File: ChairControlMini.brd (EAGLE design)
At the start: 150 x 84 mm, 36 parts, among them J1 Digital_0_7, J2 Analog, J3 Digital_8_13, J4 Analog, J5 Digital_0_7, SW1 SWITCH-DPDT3, X1 INPUT, X2 OUTPUT, X4 INPUT

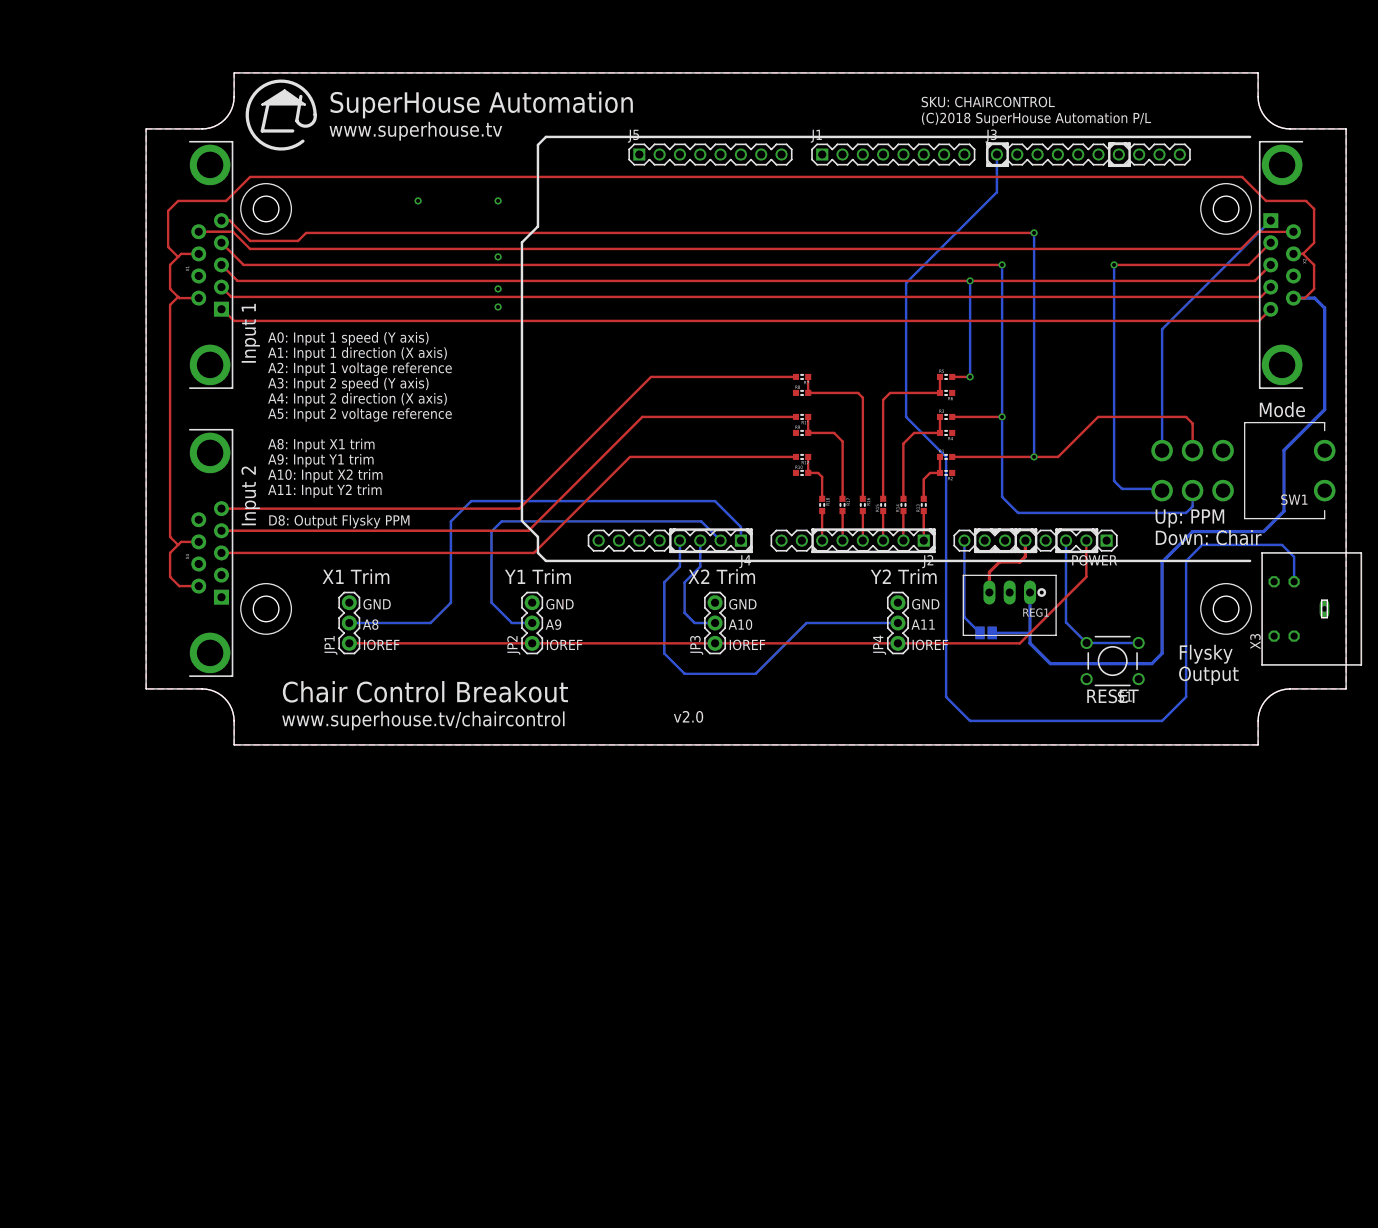
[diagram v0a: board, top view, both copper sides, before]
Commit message: Added CAN interface and removed second joystick input
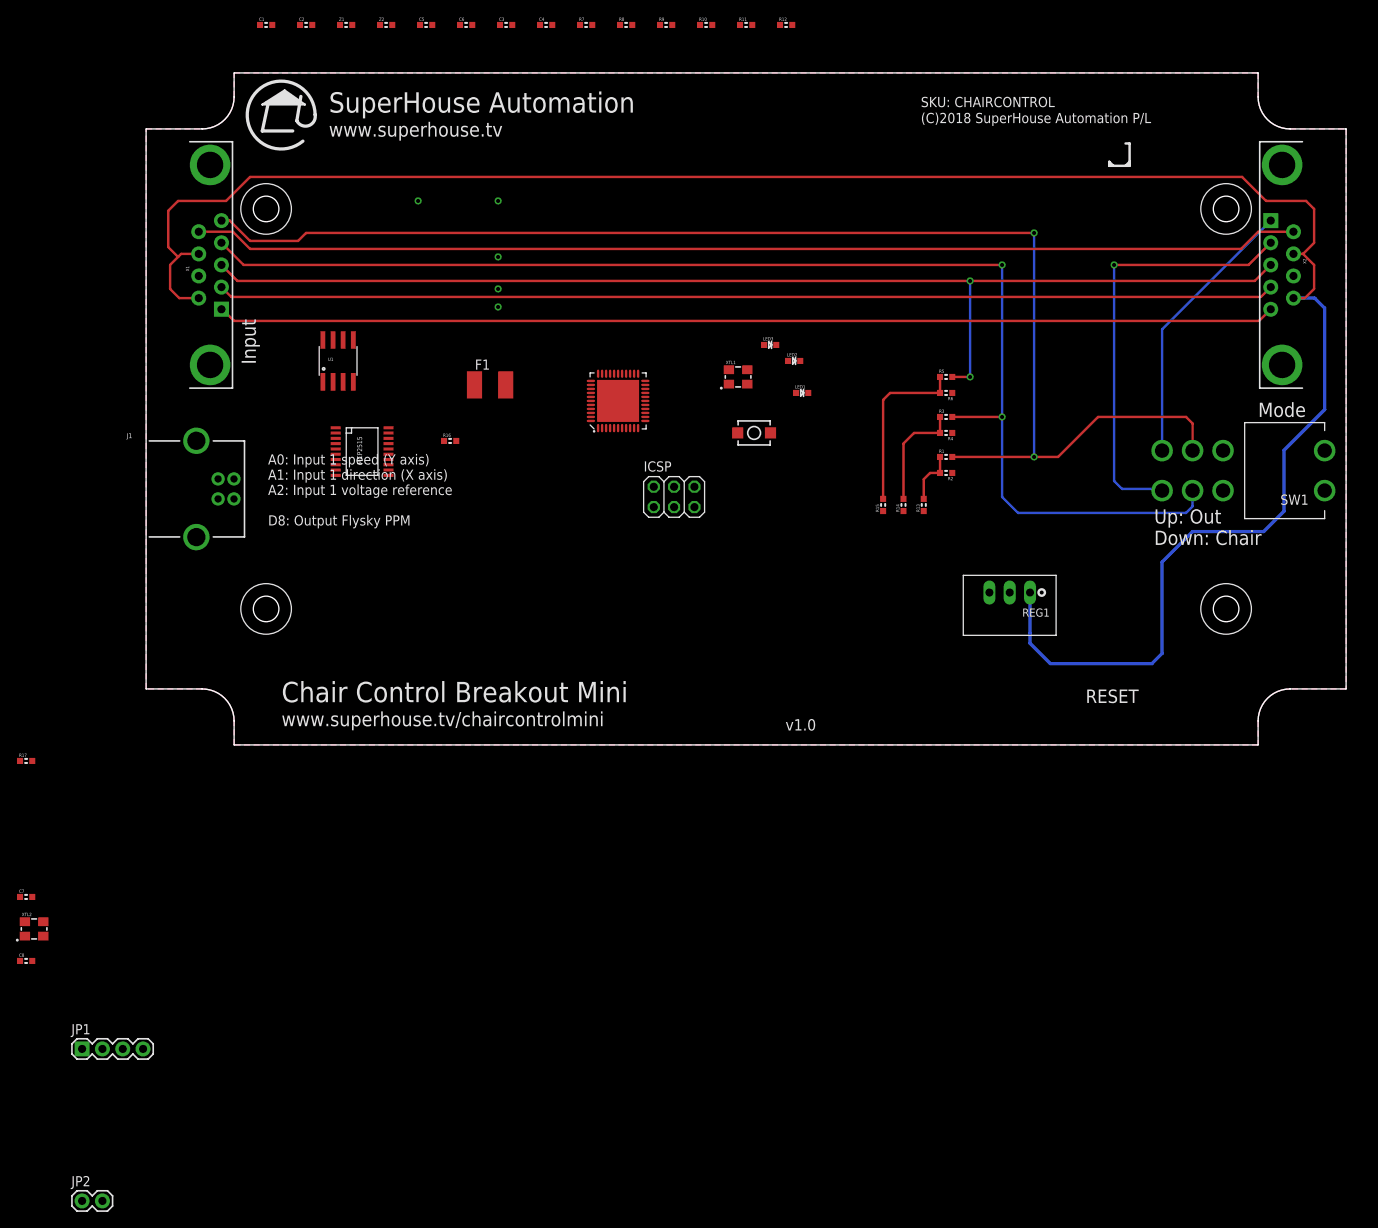
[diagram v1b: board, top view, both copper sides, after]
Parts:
- removed J2, J4: Analog, freetronics-jon:1X08
- removed J3: Digital_8_13, freetronics-original:1X10
- removed J5: Digital_0_7, freetronics:1X08
- removed JP3, JP4: (no value), freetronics-jon:1X03
- removed POWER: Power, freetronics-original:1X08
- removed R18: 1K, freetronics-jon:0603
- removed S1: RESET, freetronics:TACTILE-PTH
- removed SJ1: (no value), freetronics-jon:SJ
- removed X3: (no value), freetronics-jon:MDIN04S
- removed X4: INPUT, SparkFun-Connectors:DB9_MALE
- added C1, C2: 100nF, freetronics-master-v1.1:0603
- added C3, C4: 1uF, freetronics-master-v1.1:0603
- added C5, C6, C7, C8: 15pF, freetronics-master-v1.1:0603
- added F1: 500mA PTC 1812, rcl:L1812
- added IC1: ATMEGA32U4-QFN, freetronics-jon:QFN-44N
- added ICSP: ICSP, pinhead:2X03
- added LED1: BLUE, freetronics-jon:LED-0603
- added LED2: RED, freetronics-jon:LED-0603
- added LED3: GREEN, freetronics-jon:LED-0603
- added S21: RESET, freetronics-jon:TACTILE_SWITCH_SMD_2PIN_TINY
- added U$4: MCP2515, MCP2515:TSSOP20
- added U1: MCP2551, freetronics-original:SO08
- added XTL1, XTL2: 16MHz, freetronics-jon:CRYSTAL-SMD-3X2
- added Z1, Z2: PGB1010603, freetronics-master-v1.1:0603
- J1: value Digital_0_7 -> USB_B_PTH; device freetronics:1X08 -> SparkFun-Connectors:USB-B-PTH
- JP1: value (none) -> CAN; device freetronics-jon:1X03 -> freetronics-jon:1X04
- JP2: value (none) -> PWR; device freetronics-jon:1X03 -> freetronics-jon:1X02
- R10, R9: value 47K 1% -> 1K
- R11, R12: value 47K 1% -> 22R
- R16, R17: value 1K -> 10K; device freetronics-jon:0603 -> freetronics-master-v1.1:0603
- R7: value 47K 1% -> 10K; device freetronics-jon:0603 -> freetronics-master-v1.1:0603
- R8: value 47K 1% -> 4K7
- moved R17 106.9 mm to (-15.0, -2.00), turned to 0 degrees
- moved J1 89.8 mm to (5.00, 32.0)
- moved JP2 89.6 mm to (-8.00, -57.0), turned to 0 degrees
- moved JP1 60.7 mm to (-8.00, -38.0), turned to 0 degrees
- moved R10 57.3 mm to (70.0, 90.0)
- moved R12 54.0 mm to (80.0, 90.0), turned to 0 degrees
- moved R9 53.8 mm to (65.0, 90.0)
- moved R16 52.2 mm to (38.0, 38.0), turned to 0 degrees
- moved R7 51.6 mm to (55.0, 90.0), turned to 0 degrees
- moved R8 51.0 mm to (60.0, 90.0)
- moved R11 49.5 mm to (75.0, 90.0), turned to 0 degrees
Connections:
- removed net A10: J4.3, JP3.2
- removed net A11: J4.4, JP4.2
- removed net A8: J4.1, JP1.2
- removed net A9: J4.2, JP2.2
- removed net D0_RX: J1.1
- removed net D10: J3.3
- removed net D11_MOSI: J3.4
- removed net D12_MISO: J3.5
- removed net D13_SCK: J3.6
- removed net D1_TX: J1.2
- removed net D2: J1.3
- removed net D3: J1.4
- removed net D4: J1.5
- removed net D6: J1.7
- removed net D7: J1.8
- removed net D8: J3.1, X3.1
- removed net D9: J3.2
- removed net DIRECTION_IN_2: R11.2, X4.2
- removed net IOREF: JP1.1, JP2.1, JP3.1, JP4.1, POWER.2
- removed net NC: POWER.1
- removed net REFERENCE_2: R12.2, X4.3
- removed net SCL: J3.10
- removed net SDA: J3.9
- removed net SPEED_IN_2: R7.2, X4.1
- removed net VIN: POWER.8, SJ1.1
- new net CANH: JP1.2, U1.7
- new net CANL: JP1.3, U1.6
- new net D+: J1.D+, R12.1, Z2.2
- new net D-: J1.D-, R11.1, Z1.2
- new net D0: IC1.20
- new net D1: IC1.21
- new net D10_A11: IC1.30, U$4.18
- new net D11: IC1.12
- new net D12: IC1.26
- new net D13: IC1.32
- new net D2_SDA: IC1.19
- new net D3_SCL: IC1.18
- new net D4_A6: IC1.25
- new net D6_A8: IC1.27
- new net D7_AIN0: IC1.1
- new net D8_A9: IC1.28
- new net D9_A10: IC1.29
- new net HWB: IC1.33
- new net INT: U$4.13
- new net MISO: IC1.11, ICSP.1, U$4.17
- new net MOSI: IC1.10, ICSP.4, U$4.16
- new net N$10: R16.1, U$4.19
- new net N$11: C5.2, IC1.17, XTL1.3
- new net N$12: C6.2, IC1.16, XTL1.1
- new net N$13: U$4.2, U1.4
- new net N$14: C8.2, U$4.9, XTL2.1
- new net N$15: JP1.1, JP2.2
- new net N$16: R17.2, U1.8
- new net N$18: C7.2, U$4.8, XTL2.3
- new net N$5: LED1.A, R8.1
- new net RD+: IC1.4, R12.2
- new net RD-: IC1.3, R11.2
- new net RXLED_SS: IC1.8, LED3.C
- new net SCK: IC1.9, ICSP.3, U$4.14
- new net TX_LED: IC1.22, LED2.C
- new net USB+: F1.1, J1.VBUS
- net 12V: now also JP2.1; no longer SJ1.2, X4.7, X4.9
- net 3V3: now also C4.2, IC1.6; no longer POWER.4
- net 5V: now also C2.1, C3.1, F1.2, IC1.14, IC1.2, IC1.24, IC1.34, IC1.44, IC1.7, ICSP.2, R10.2, R16.2, R7.2, R8.2, R9.2, U$4.20, U1.3; no longer POWER.5
- net A0: now also IC1.36; no longer J2.1
- net A1: now also IC1.37; no longer J2.2
- net A2: now also IC1.38; no longer J2.3
- net A3: now also IC1.39; no longer J2.4, R16.2
- net A4: now also IC1.40; no longer J2.5, R17.2
- net A5: now also IC1.41; no longer J2.6, R18.2
- net AREF: now also C1.1, IC1.42; no longer J3.8
- net D5: now also IC1.31; no longer J1.6
- net GND: now also C1.2, C2.2, C3.2, C4.1, C5.1, C6.1, C7.1, C8.1, IC1.15, IC1.23, IC1.35, IC1.43, IC1.5, IC1.TGND, ICSP.6, J1.GND, J1.SHLD1, J1.SHLD2, JP1.4, LED1.C, R17.1, S21.1, U$4.10, U1.2, XTL1.2, XTL1.4, XTL2.2, XTL2.4, Z1.1, Z2.1; no longer J3.7, JP1.3, JP2.3, JP3.3, JP4.3, POWER.6, POWER.7, R10.1, R8.1, R9.1, S1.1, S1.2, X3.M, X4.8
- net N$7: now also LED2.A, R9.1; no longer R16.1, R7.1, R8.2
- net N$8: now also LED3.A, R10.1; no longer R11.1, R17.1, R9.2
- net N$9: now also U$4.1, U1.1; no longer R10.2, R12.1, R18.1
- net RESET: now also IC1.13, ICSP.5, R7.1, S21.2; no longer POWER.3, S1.3, S1.4
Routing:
- net D8: track 142.1 -> 0.00 mm
- net IOREF: track 100.1 -> 0.00 mm
- net SPEED_IN_2: track 78.6 -> 0.00 mm
- net DIRECTION_IN_2: track 77.7 -> 0.00 mm
- net REFERENCE_2: track 76.8 -> 0.00 mm
- net A8: track 64.3 -> 0.00 mm
- net A11: track 47.8 -> 0.00 mm
- net 12V: track 313.0 -> 265.2 mm
- net A9: track 45.2 -> 0.00 mm
- net N$7: track 21.7 -> 0.00 mm
- net RESET: track 20.4 -> 0.00 mm
- net A10: track 14.2 -> 0.00 mm
- net N$8: track 13.9 -> 0.00 mm
- net VIN: track 12.3 -> 0.00 mm
- net 5V: track 9.84 -> 0.00 mm
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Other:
- board text added: "A0: Input 1 speed (Y axis) A1: Input 1 direction (X axis) A2: Input 1 voltage reference D8: Output Flysky PPM"
- board text added: "Chair Control Breakout Mini"
- board text added: "Input"
- board text added: "Up: Out Down: Chair"
- board text added: "v1.0"
- board text added: "www.superhouse.tv/chaircontrolmini"
- board text removed: "A0: Input 1 speed (Y axis) A1: Input 1 direction (X axis) A2: Input 1 voltage reference A3: Input 2 speed (Y axis) A4: Input 2 direction (X axis) A5: Input 2 voltage reference A8: Input X1 trim A9: Input Y1 trim A10: Input X2 trim A11: Input Y2 trim D8: Output Flysky PPM"
- board text removed: "A10"
- board text removed: "A11"
- board text removed: "A8"
- board text removed: "A9"
- board text removed: "Chair Control Breakout"
- board text removed: "Flysky Output"
- board text removed: "GND"
- board text removed: "IOREF"
- board text removed: "Input 1"
- board text removed: "Input 2"
- board text removed: "Up: PPM Down: Chair"
- board text removed: "X1 Trim"
- board text removed: "X2 Trim"
- board text removed: "Y1 Trim"
- board text removed: "Y2 Trim"
- board text removed: "v2.0"
- board text removed: "www.superhouse.tv/chaircontrol"

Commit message: Added power source selection and DRC for v1.0 release
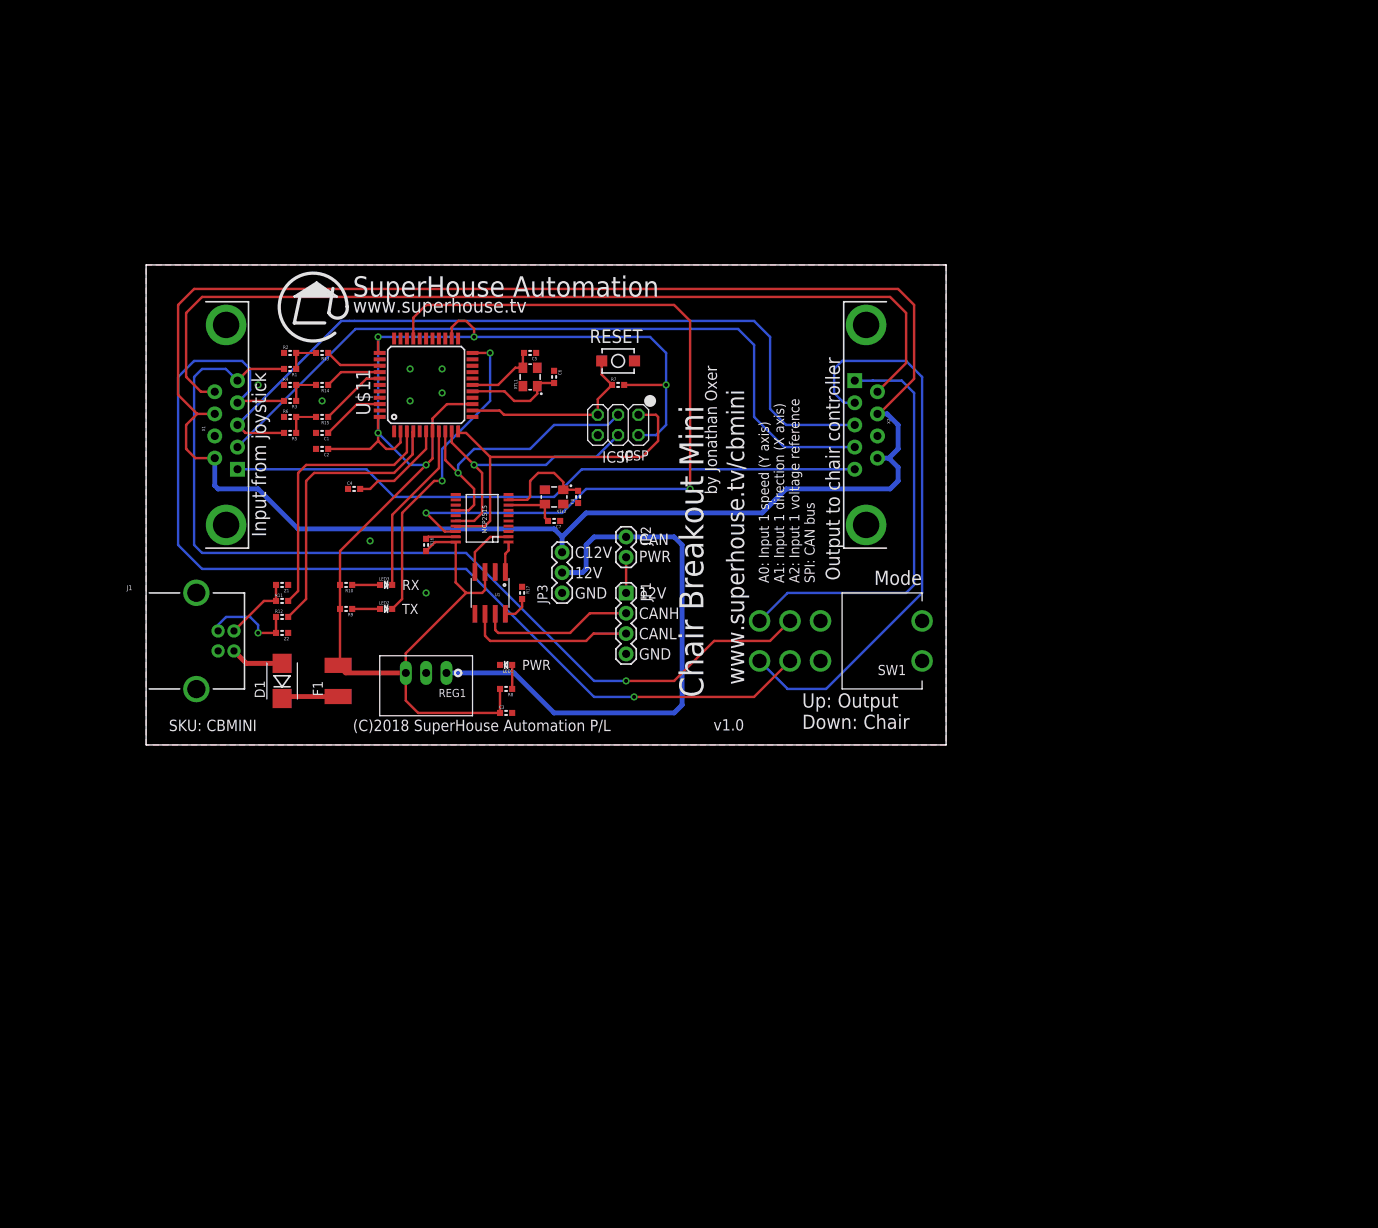
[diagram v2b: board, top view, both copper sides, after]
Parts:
- removed IC1: ATMEGA32U4-QFN, freetronics-jon:QFN-44N
- added D1: 1N4004, freetronics-jon:SMB-DIODE
- added JP3: PWR, freetronics-jon:1X03
- added U$11: ATMEGA32U4NT, freetronics-jon:TQFP44
- XTL2: value 16MHz -> 8MHz
- moved JP2 107.3 mm to (60.0, 26.0), turned to 270 degrees
- moved R12 97.2 mm to (17.0, 16.0)
- moved R11 92.5 mm to (17.0, 18.0)
- moved C8 90.1 mm to (54.0, 31.0), turned to 90 degrees
- moved JP1 88.7 mm to (60.0, 19.0), turned to 270 degrees
- moved C3 86.0 mm to (45.0, 4.00)
- moved XTL2 84.5 mm to (51.0, 31.0), turned to 180 degrees
- moved R8 84.3 mm to (45.0, 7.00), turned to 180 degrees
- moved R2 83.4 mm to (18.0, 49.0), turned to 0 degrees
- moved R9 83.2 mm to (25.0, 17.0), turned to 180 degrees
- moved R10 83.2 mm to (25.0, 20.0), turned to 180 degrees
- moved R1 82.7 mm to (18.0, 47.0), turned to 180 degrees
- moved R5 82.3 mm to (18.0, 39.0), turned to 180 degrees
- moved R4 82.2 mm to (18.0, 45.0), turned to 0 degrees
- moved R6 82.1 mm to (18.0, 41.0), turned to 0 degrees
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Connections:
- new net C12V: JP3.3, X1.7, X1.9, X2.7, X2.9
- new net N$17: D1.C, F1.1
- net 12V: now also JP3.2; no longer X1.7, X1.9, X2.7, X2.9
- net 3V3: now also U$11.6; no longer IC1.6
- net 5V: now also U$11.14, U$11.2, U$11.24, U$11.34, U$11.44, U$11.7; no longer IC1.14, IC1.2, IC1.24, IC1.34, IC1.44, IC1.7
- net A0: now also U$11.36; no longer IC1.36
- net A1: now also U$11.37; no longer IC1.37
- net A2: now also U$11.38; no longer IC1.38
- net A3: now also U$11.39; no longer IC1.39
- net A4: now also U$11.40; no longer IC1.40
- net A5: now also U$11.41; no longer IC1.41
- net AREF: now also U$11.42; no longer IC1.42
- net D0: now also U$11.20; no longer IC1.20
- net D1: now also U$11.21; no longer IC1.21
- net D10_A11: now also U$11.30; no longer IC1.30
- net D11: now also U$11.12; no longer IC1.12
- net D12: now also U$11.26; no longer IC1.26
- net D13: now also U$11.32; no longer IC1.32
- net D2_SDA: now also U$11.19; no longer IC1.19
- net D3_SCL: now also U$11.18; no longer IC1.18
- net D4_A6: now also U$11.25; no longer IC1.25
- net D5: now also U$11.31; no longer IC1.31
- net D6_A8: now also U$11.27; no longer IC1.27
- net D7_AIN0: now also U$11.1; no longer IC1.1
- net D8_A9: now also U$11.28; no longer IC1.28
- net D9_A10: now also U$11.29; no longer IC1.29
- net GND: now also JP3.1, U$11.15, U$11.23, U$11.35, U$11.43, U$11.5; no longer IC1.15, IC1.23, IC1.35, IC1.43, IC1.5, IC1.TGND
- net HWB: now also U$11.33; no longer IC1.33
- net MISO: now also U$11.11; no longer IC1.11
- net MOSI: now also U$11.10; no longer IC1.10
- net N$11: now also U$11.17; no longer IC1.17
- net N$12: now also U$11.16; no longer IC1.16
- net RD+: now also U$11.4; no longer IC1.4
- net RD-: now also U$11.3; no longer IC1.3
- net RESET: now also U$11.13; no longer IC1.13
- net RXLED_SS: now also U$11.8; no longer IC1.8
- net SCK: now also U$11.9; no longer IC1.9
- net TX_LED: now also U$11.22; no longer IC1.22
- net USB+: now also D1.A; no longer F1.1
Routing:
- net C12V: track 0.00 -> 244.0 mm
- net 5V: track 0.00 -> 195.6 mm, vias 0 -> 5
- net 12V: track 265.2 -> 71.0 mm
- net D10_A11: track 0.00 -> 98.6 mm, vias 0 -> 2
- net DETECT: track 132.4 -> 80.0 mm
- net SPEED_IN: track 166.9 -> 118.5 mm, vias 2 -> 1
- net REFERENCE: track 147.1 -> 99.4 mm, vias 2 -> 0
- net MISO: track 0.00 -> 45.3 mm
- net TX_LED: track 0.00 -> 39.9 mm, vias 0 -> 2
- net N$6: track 132.2 -> 94.7 mm
- net SCK: track 0.00 -> 36.9 mm, vias 0 -> 1
- net RD+: track 0.00 -> 35.5 mm
- net MOSI: track 0.00 -> 35.0 mm, vias 0 -> 1
- net RD-: track 0.00 -> 33.8 mm
- net DIRECTION_IN: track 160.9 -> 128.3 mm, vias 2 -> 1
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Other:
- board size 150 x 84 mm -> 100 x 60 mm
- board text added: "12V"
- board text added: "A0: Input 1 speed (Y axis) A1: Input 1 direction (X axis) A2: Input 1 voltage reference SPI: CAN bus"
- board text added: "C12V"
- board text added: "CAN PWR"
- board text added: "CANH"
- board text added: "CANL"
- board text added: "Chair Breakout Mini"
- board text added: "GND"
- board text added: "ICSP"
- board text added: "Input from joystick"
- board text added: "Output to chair controller"
- board text added: "PWR"
- board text added: "RX"
- board text added: "SKU: CBMINI"
- board text added: "TX"
- board text added: "Up: Output Down: Chair"
- board text added: "by Jonathan Oxer"
- board text added: "www.superhouse.tv/cbmini"
- board text removed: "A0: Input 1 speed (Y axis) A1: Input 1 direction (X axis) A2: Input 1 voltage reference D8: Output Flysky PPM"
- board text removed: "Chair Control Breakout Mini"
- board text removed: "Input"
- board text removed: "SKU: CHAIRCONTROL"
- board text removed: "Up: Out Down: Chair"
- board text removed: "www.superhouse.tv/chaircontrolmini"
